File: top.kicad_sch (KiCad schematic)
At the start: 0 parts

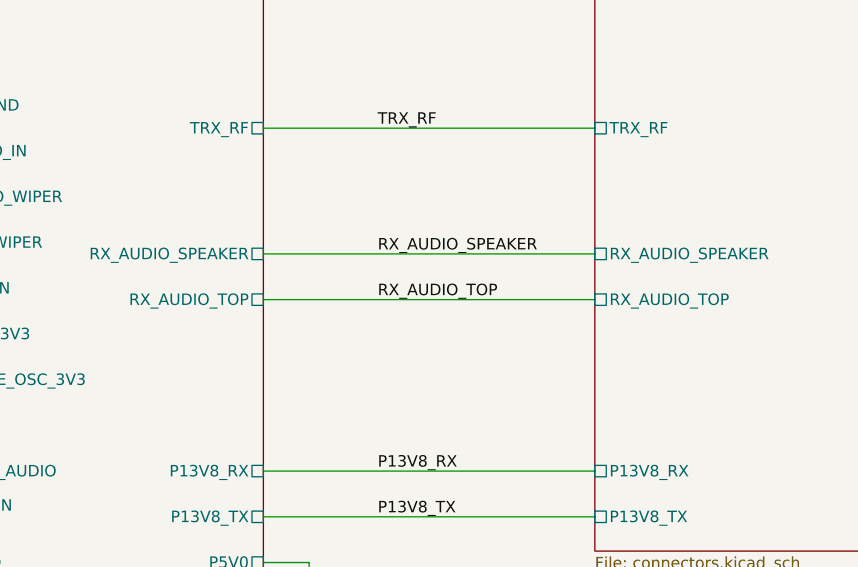
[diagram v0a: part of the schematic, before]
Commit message: trx_mobo_concept_2_B. Change design to use a dedicated 8V supply for the 2SC3357 parts. Add S-Meter connector. Change mic connector to 3 pins and add 8V sopower supply to pin 3.
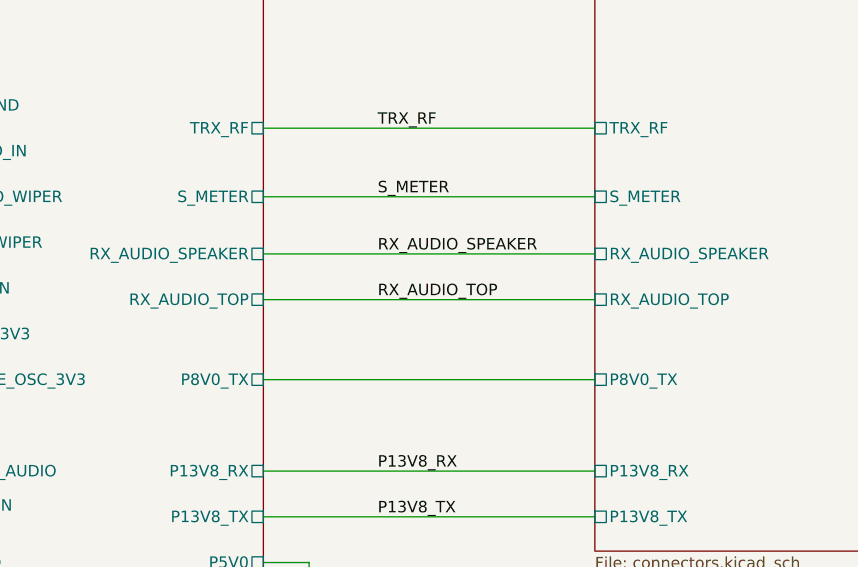
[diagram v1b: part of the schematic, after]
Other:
- sheet connectors ports: added P8V0_TX, S_METER; removed none
- sheet radio ports: added P8V0_TX, S_METER; removed none
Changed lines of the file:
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@@
   (title_block
     (title "Top")
-    (rev "X1")
+    (rev "B")
     (company "WA6ZFT")
   )
+  (wire (pts (xy 153.67 73.66) (xy 190.5 73.66))
+    (stroke (width 0) (type default) (color 0 0 0 0))
+  )
   (wire (pts (xy 114.3 83.82) (xy 76.2 83.82))
     (stroke (width 0) (type default) (color 0 0 0 0))
@@
   )
   (wire (pts (xy 190.5 80.01) (xy 153.67 80.01))
+    (stroke (width 0) (type default) (color 0 0 0 0))
+  )
+  (wire (pts (xy 153.67 93.98) (xy 190.5 93.98))
     (stroke (width 0) (type default) (color 0 0 0 0))
   )
@@
   )
   (label "RX_AUDIO_TOP" (at 166.37 85.09 0)
+    (effects (font (size 1.27 1.27)) (justify left bottom))
+  )
+  (label "S_METER" (at 166.37 73.66 0)
     (effects (font (size 1.27 1.27)) (justify left bottom))
   )
@@
       (effects (font (size 1.27 1.27)) (justify left))
     )
+    (pin "S_METER" passive (at 153.67 73.66 0)
+      (effects (font (size 1.27 1.27)) (justify right))
+    )
+    (pin "P8V0_TX" passive (at 153.67 93.98 0)
+      (effects (font (size 1.27 1.27)) (justify right))
+    )
   )
   (sheet (at 190.5 50.8) (size 50.8 62.23) (fields_autoplaced)
@@
       (effects (font (size 1.27 1.27)) (justify right))
     )
-  )
+    (pin "S_METER" passive (at 190.5 73.66 180)
+      (effects (font (size 1.27 1.27)) (justify left))
+    )
+    (pin "P8V0_TX" passive (at 190.5 93.98 180)
+      (effects (font (size 1.27 1.27)) (justify left))
+    )
+  )
